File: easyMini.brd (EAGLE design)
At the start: 100 x 80 mm, 32 parts

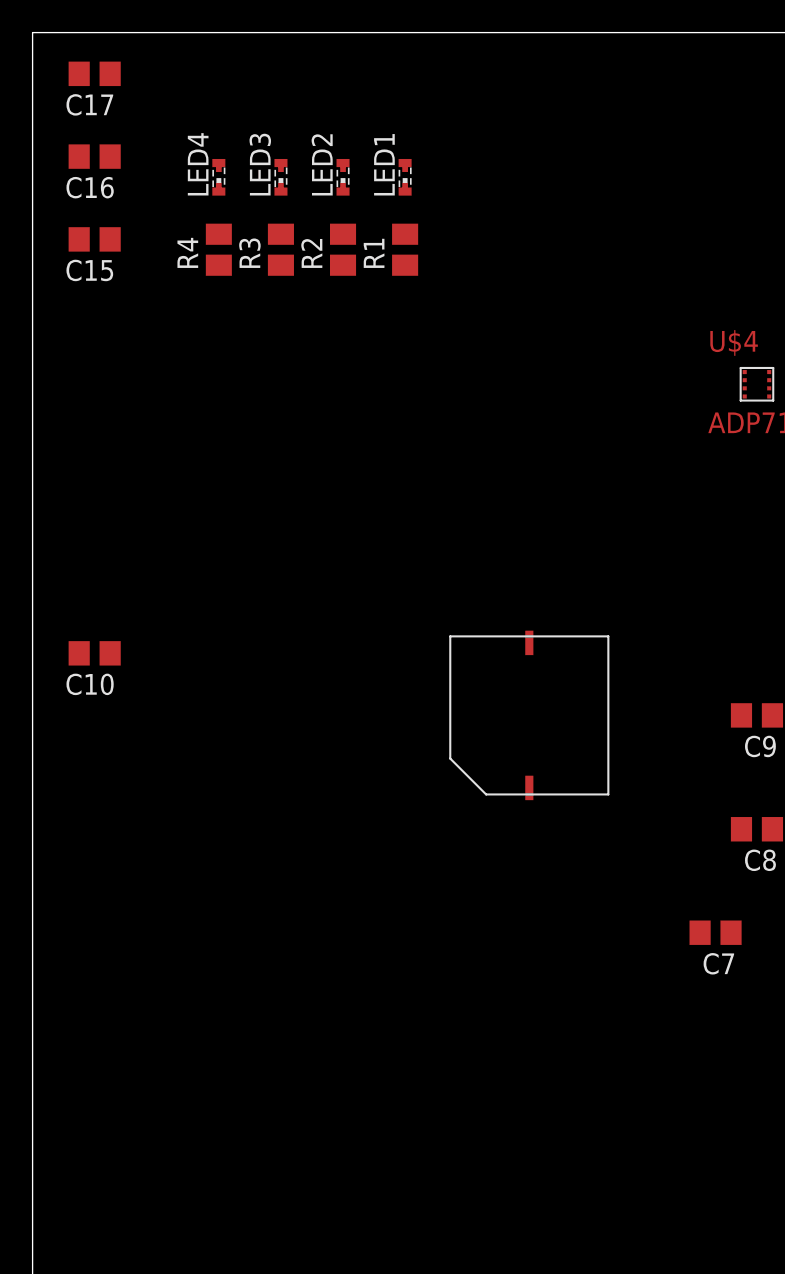
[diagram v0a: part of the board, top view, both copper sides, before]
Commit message: Added pyro fets, resistors, and connectors. Modified board design to make more compact.
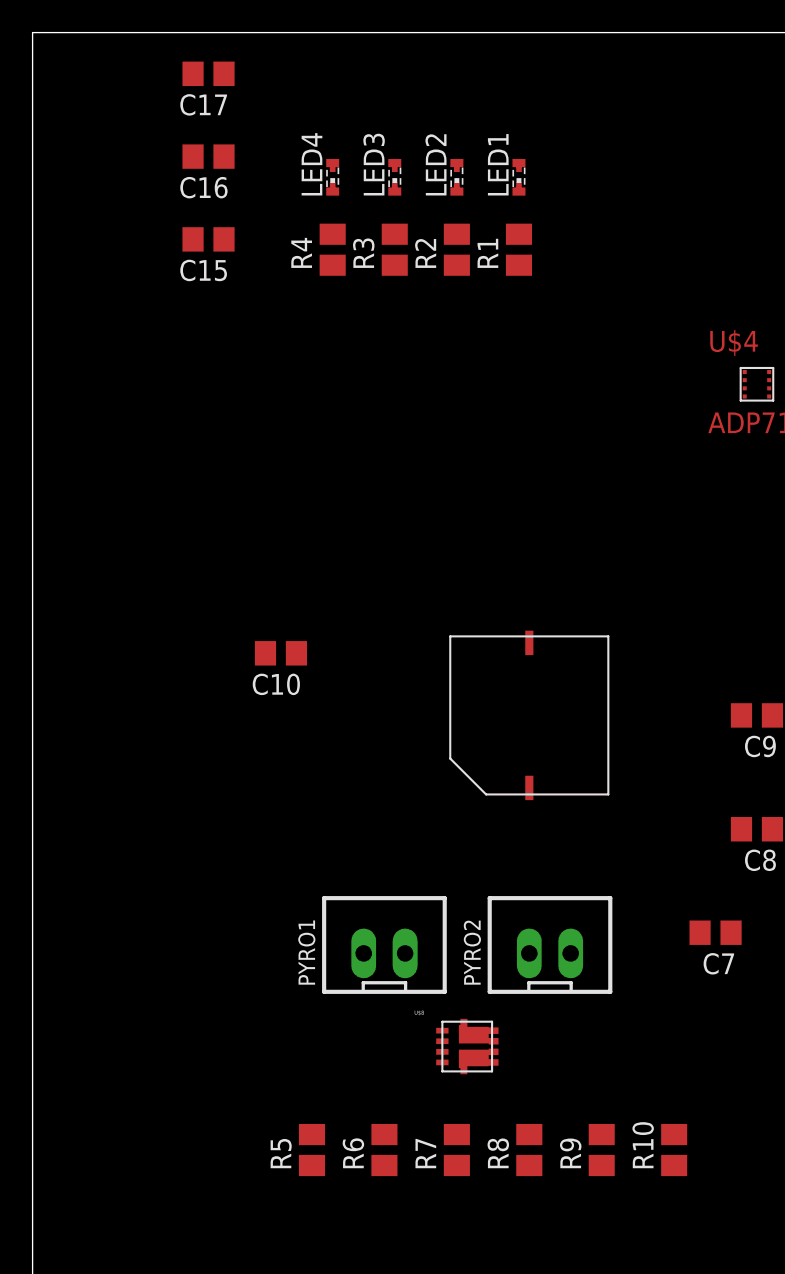
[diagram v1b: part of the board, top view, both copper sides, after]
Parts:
- added PYRO1, PYRO2: JST-XH-02-PIN-LONG-PAD, Rembrandt Electronics - JST XH Connectors v1-0:JST-XH-02-PACKAGE-LONG-PAD
- added R10, R5, R6, R7, R8, R9: (no value), rcl:M0805
- added U$8: SI7232DN, generalUse:SI7232DN
- C9: value (none) -> 4.7 pF
- moved C10 11.4 mm to (15.2, 41.9)
- moved LED3 6.99 mm to (22.2, 71.1)
- moved R3 6.99 mm to (22.2, 66.7)
- moved C15 6.98 mm to (10.8, 67.3)
- moved C16 6.98 mm to (10.8, 72.4)
- moved C17 6.98 mm to (10.8, 77.5)
- moved LED1 6.98 mm to (29.8, 71.1)
- moved LED2 6.98 mm to (26.0, 71.1)
- moved LED4 6.98 mm to (18.4, 71.1)
- moved R1 6.98 mm to (29.8, 66.7)
- moved R2 6.98 mm to (26.0, 66.7)
- moved R4 6.98 mm to (18.4, 66.7)
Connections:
- new net N$14: PYRO1.2, R7.1, U$8.8
- new net N$17: PYRO2.2, R8.1, U$8.6
- new net N$18: R6.2, U$1.26, U$8.2
- new net N$19: R5.2, U$1.27, U$8.4
- new net N$21: R7.2, R9.2, U$1.28
- new net N$22: R10.2, R8.2, U$1.29
- net +3V3: now also PYRO1.1, PYRO2.1
- net GND: now also C13.2, C14.2, R10.1, R5.1, R6.1, R9.1, U$8.1, U$8.3; no longer C13.1, C14.1
- net N$4: now also C13.1; no longer C13.2
- net N$5: now also C14.1; no longer C14.2

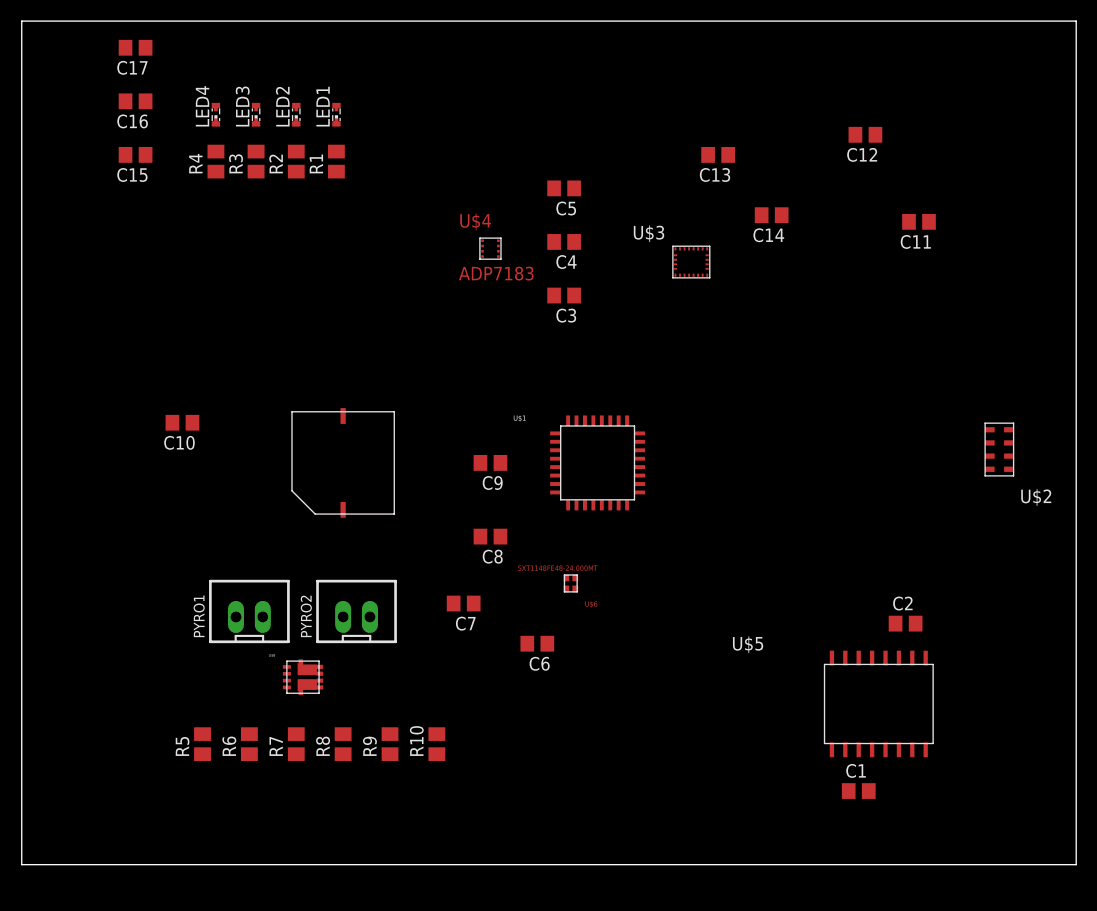
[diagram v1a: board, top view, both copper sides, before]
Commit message: Added reverse polarity protection and battery/switch connectors. Continued board design organization:
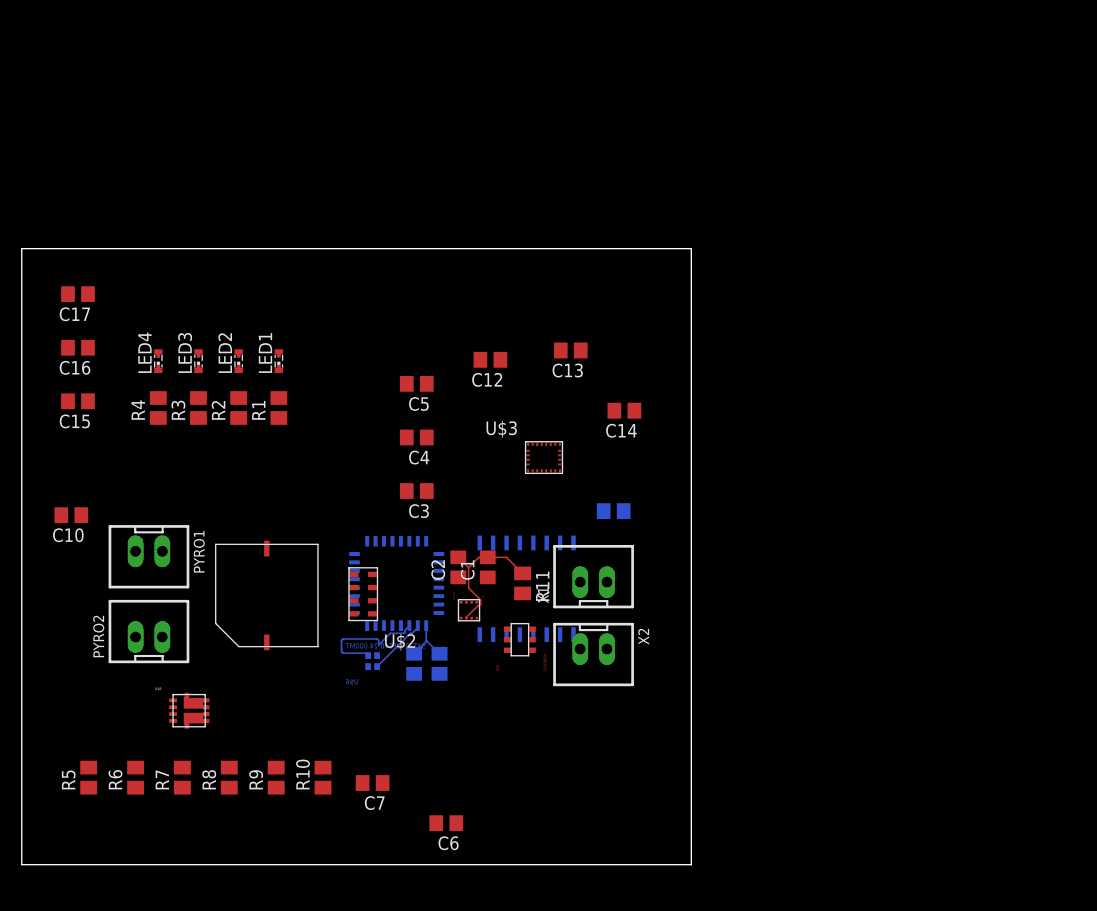
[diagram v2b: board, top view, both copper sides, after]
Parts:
- added R11: (no value), rcl:M0805
- added U$9: SI3429EDV, generalUse:SI3429EDV
- added X1, X2: JST-XH-02-PIN-LONG-PAD, Rembrandt Electronics - JST XH Connectors v1-0:JST-XH-02-PACKAGE-LONG-PAD
- moved U$2 61.9 mm to (32.4, 25.7)
- moved C2 42.8 mm to (41.4, 28.2), turned to 90 degrees
- moved C12 41.5 mm to (44.5, 47.9)
- moved C1 41.1 mm to (44.2, 28.2), turned to 90 degrees
- moved C11 39.9 mm to (56.1, 33.5), flipped to the bottom
- moved U$5 35.1 mm to (47.9, 26.2), flipped to the bottom
- moved U$4 34.4 mm to (42.4, 24.1), turned to 270 degrees
- moved C15 24.0 mm to (5.33, 43.9)
- moved C16 24.0 mm to (5.33, 49.0)
- moved C17 24.0 mm to (5.33, 54.1)
- moved LED1 24.0 mm to (24.4, 47.8)
- moved LED2 24.0 mm to (20.6, 47.8)
- moved LED3 24.0 mm to (16.8, 47.8)
- moved LED4 24.0 mm to (13.0, 47.8)
- moved R1 24.0 mm to (24.4, 43.3)
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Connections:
- new net N$23: X1.2, X2.1
- new net N$26: R11.2, U$9.3, X1.1
- new net N$27: U$9.1, X2.2
- net GND: now also R11.1
- net VCC: now also U$9.4
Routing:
- net GND: track 0.00 -> 13.4 mm
- net N$25: track 0.00 -> 11.6 mm
- net N$24: track 0.00 -> 5.59 mm
- net +3V3: track 0.00 -> 4.93 mm
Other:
- board size 100 x 80 mm -> 63.5 x 58.4 mm

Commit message: Shrink board and organization of two layers into more sensible layout. Changed pins to allow USB addition on microcontroller.
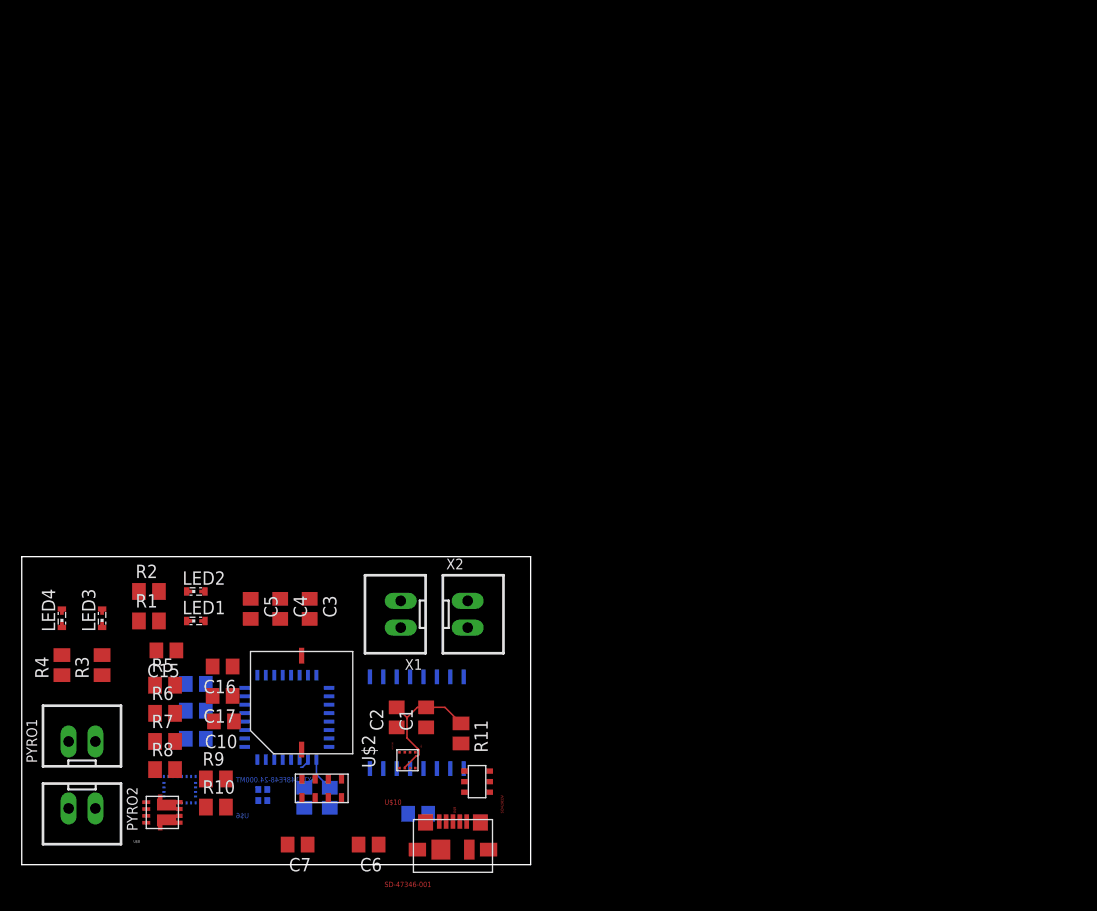
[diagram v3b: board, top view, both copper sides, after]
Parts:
- added U$10: SD-47346-001, generalUse:SD-47346-001
- moved C13 51.2 mm to (16.5, 11.9), flipped to the bottom
- moved C14 49.6 mm to (16.5, 14.6), flipped to the bottom
- moved U$3 46.7 mm to (15.0, 7.11), flipped to the bottom
- moved C12 41.5 mm to (16.5, 17.1), flipped to the bottom
- moved C17 40.5 mm to (19.1, 16.0)
- moved C11 34.2 mm to (37.6, 4.83)
- moved C16 33.2 mm to (19.1, 18.8)
- moved C5 26.5 mm to (21.7, 24.3), turned to 270 degrees
- moved LED3 26.0 mm to (7.62, 23.4)
- moved LED4 26.0 mm to (3.81, 23.4)
- moved R3 26.0 mm to (7.62, 18.9)
- moved R4 26.0 mm to (3.81, 18.9)
- moved LED1 25.9 mm to (16.5, 23.1), turned to 270 degrees
- moved C15 25.1 mm to (13.7, 20.3)
- moved C10 24.3 mm to (19.2, 13.6)
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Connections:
- new net N$28: U$1.21, U$10.2
- new net N$29: U$1.22, U$10.3
- net GND: now also U$10.10, U$10.11, U$10.5, U$10.6, U$10.7, U$10.8, U$10.9
- net N$15: now also U$1.24; no longer U$1.21
- net N$16: now also U$1.25; no longer U$1.22
- net N$9: now also U$1.23; no longer U$1.20
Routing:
- net N$25: track 11.6 -> 0.32 mm
- net N$24: track 5.59 -> 1.12 mm
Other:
- board size 63.5 x 58.4 mm -> 48.3 x 29.2 mm
